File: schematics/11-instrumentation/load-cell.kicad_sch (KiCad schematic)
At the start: 12 parts, among them IC1 HX711, Q1 S8550

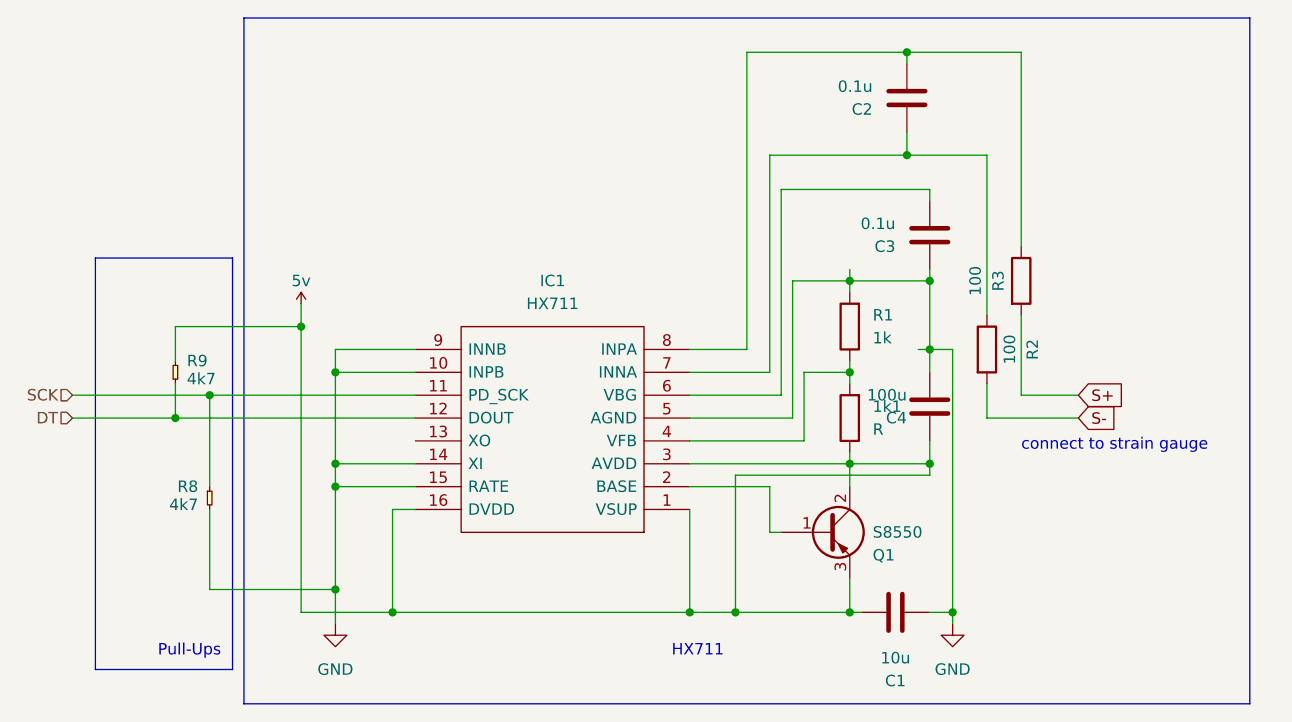
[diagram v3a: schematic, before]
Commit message: load cell schematic
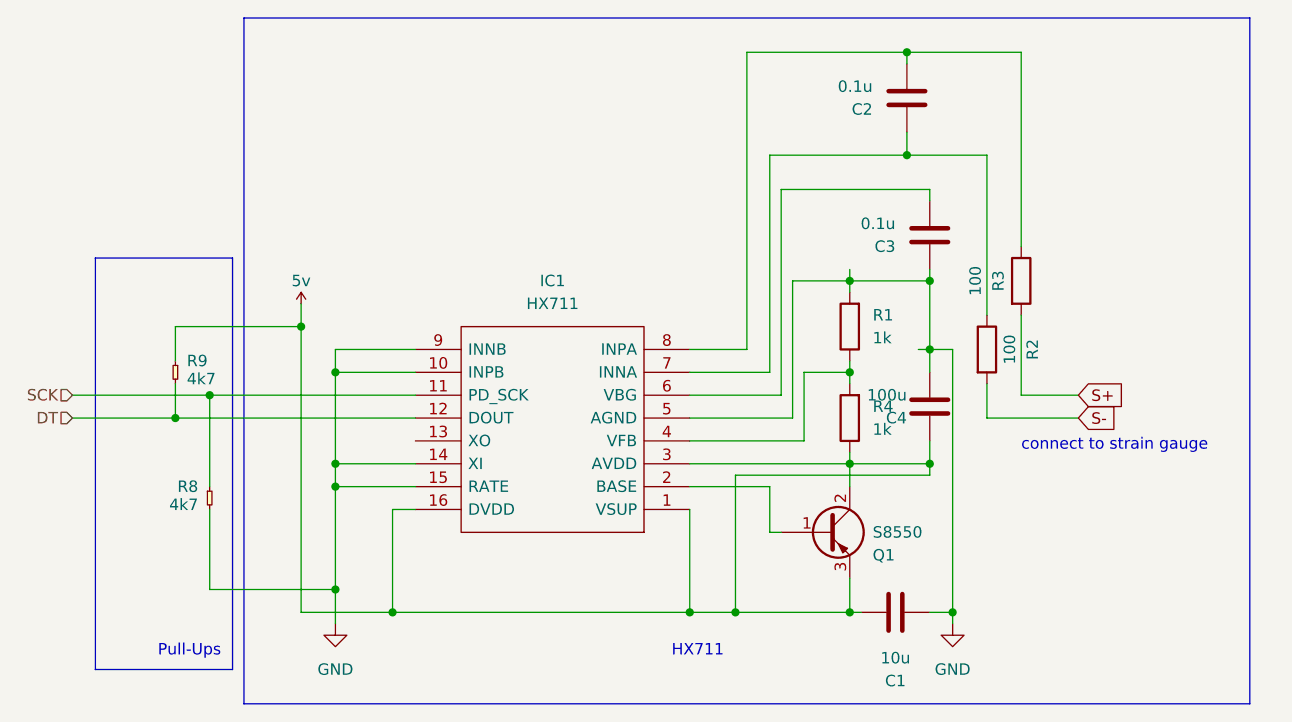
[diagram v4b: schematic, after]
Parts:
- C1, C2, C3, C4: footprint (none) -> royale:C_0402_1005Metric_Pad0.74x0.62mm_HandSolder
- IC1: footprint SOIC127P600X160-16N -> hx711:SOIC127P600X160-16N
- Q1: footprint (none) -> s8850:MJE13001TP
- R1, R2, R3, R8, R9: footprint (none) -> royale:R_0402_1005Metric_Pad0.72x0.64mm_HandSolder
- R4: renamed from 1k1; value R -> 1k; footprint (none) -> royale:R_0402_1005Metric_Pad0.72x0.64mm_HandSolder
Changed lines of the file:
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@@
+    (stroke (width 0) (type default) (color 0 0 0 0))
+  )
+  (wire (pts (xy 170.18 95.25) (xy 170.18 96.52))
     (stroke (width 0) (type default) (color 0 0 0 0))
   )
@@
     (stroke (width 0) (type default) (color 0 0 0 0))
   )
+  (wire (pts (xy 152.4 96.52) (xy 170.18 96.52))
+    (stroke (width 0) (type default) (color 0 0 0 0))
+  )
   (wire (pts (xy 119.38 101.6) (xy 119.38 113.03))
     (stroke (width 0) (type default) (color 0 0 0 0))
@@
     (stroke (width 0) (type default) (color 0 0 0 0))
   )
-  (wire (pts (xy 170.18 96.52) (xy 170.18 95.25))
-    (stroke (width 0) (type default) (color 0 0 0 0))
-  )
   (wire (pts (xy 181.61 83.82) (xy 179.07 83.82))
     (stroke (width 0) (type default) (color 0 0 0 0))
@@
   )
   (wire (pts (xy 162.56 88.9) (xy 152.4 88.9))
-    (stroke (width 0) (type default) (color 0 0 0 0))
-  )
-  (wire (pts (xy 170.18 96.52) (xy 152.4 96.52))
     (stroke (width 0) (type default) (color 0 0 0 0))
   )
@@
       (effects (font (size 1.27 1.27)) (justify left top))
     )
-    (property "Footprint" "" (id 2) (at 95.25 85.09 0)
+    (property "Footprint" "royale:R_0402_1005Metric_Pad0.72x0.64mm_HandSolder" (id 2) (at 95.25 85.09 0)
       (effects (font (size 1.27 1.27)) hide)
     )
@@
       (effects (font (size 1.27 1.27)) (justify left top))
     )
-    (property "Footprint" "" (id 2) (at 99.06 99.06 0)
+    (property "Footprint" "royale:R_0402_1005Metric_Pad0.72x0.64mm_HandSolder" (id 2) (at 99.06 99.06 0)
       (effects (font (size 1.27 1.27)) hide)
     )
@@
       (effects (font (size 1.27 1.27)) (justify left))
     )
-    (property "Footprint" "" (id 2) (at 178.1048 86.36 0)
+    (property "Footprint" "royale:C_0402_1005Metric_Pad0.74x0.62mm_HandSolder" (id 2) (at 178.1048 86.36 0)
       (effects (font (size 1.27 1.27)) hide)
     )
@@
       (effects (font (size 1.27 1.27)) (justify left))
     )
-    (property "Footprint" "" (id 2) (at 178.1048 67.31 0)
+    (property "Footprint" "royale:C_0402_1005Metric_Pad0.74x0.62mm_HandSolder" (id 2) (at 178.1048 67.31 0)
       (effects (font (size 1.27 1.27)) hide)
     )
@@
     (property "Reference" "R3" (id 0) (at 186.69 76.2 90))
     (property "Value" "100" (id 1) (at 184.15 76.2 90))
-    (property "Footprint" "" (id 2) (at 187.452 76.2 90)
+    (property "Footprint" "royale:R_0402_1005Metric_Pad0.72x0.64mm_HandSolder" (id 2) (at 187.452 76.2 90)
       (effects (font (size 1.27 1.27)) hide)
     )
@@
     (property "Reference" "IC1" (id 0) (at 137.16 76.2 0))
     (property "Value" "HX711" (id 1) (at 137.16 78.74 0))
-    (property "Footprint" "SOIC127P600X160-16N" (id 2) (at 125.73 104.14 0)
+    (property "Footprint" "hx711:SOIC127P600X160-16N" (id 2) (at 125.73 104.14 0)
       (effects (font (size 1.27 1.27)) (justify left) hide)
     )
@@
       (effects (font (size 1.27 1.27)) (justify left))
     )
-    (property "Footprint" "" (id 2) (at 172.72 101.6 0)
+    (property "Footprint" "s8850:MJE13001TP" (id 2) (at 172.72 101.6 0)
       (effects (font (size 1.27 1.27)) hide)
     )
@@
       (effects (font (size 1.27 1.27)) (justify left))
     )
-    (property "Footprint" "" (id 2) (at 175.5648 52.07 0)
+    (property "Footprint" "royale:C_0402_1005Metric_Pad0.74x0.62mm_HandSolder" (id 2) (at 175.5648 52.07 0)
       (effects (font (size 1.27 1.27)) hide)
     )
@@
   )
   (symbol (lib_id "Device:R") (at 170.18 91.44 180) (unit 1)
-    (in_bom yes) (on_board yes) (fields_autoplaced)
-    (property "Reference" "1k1" (id 0) (at 172.72 90.1699 0)
+    (in_bom yes) (on_board yes)
+    (property "Reference" "R4" (id 0) (at 172.72 90.1699 0)
       (effects (font (size 1.27 1.27)) (justify right))
     )
-    (property "Value" "R" (id 1) (at 172.72 92.7099 0)
+    (property "Value" "1k" (id 1) (at 172.72 92.7099 0)
       (effects (font (size 1.27 1.27)) (justify right))
     )
-    (property "Footprint" "" (id 2) (at 171.958 91.44 90)
+    (property "Footprint" "royale:R_0402_1005Metric_Pad0.72x0.64mm_HandSolder" (id 2) (at 171.958 91.44 90)
       (effects (font (size 1.27 1.27)) hide)
     )
@@
       (effects (font (size 1.27 1.27)) (justify right))
     )
-    (property "Footprint" "" (id 2) (at 171.958 81.28 90)
+    (property "Footprint" "royale:R_0402_1005Metric_Pad0.72x0.64mm_HandSolder" (id 2) (at 171.958 81.28 90)
       (effects (font (size 1.27 1.27)) hide)
     )
@@
     (property "Reference" "R2" (id 0) (at 190.5 83.82 90))
     (property "Value" "100" (id 1) (at 187.96 83.82 90))
-    (property "Footprint" "" (id 2) (at 183.642 83.82 90)
+    (property "Footprint" "royale:R_0402_1005Metric_Pad0.72x0.64mm_HandSolder" (id 2) (at 183.642 83.82 90)
       (effects (font (size 1.27 1.27)) hide)
     )
@@
     (property "Reference" "C1" (id 0) (at 175.26 120.65 90))
     (property "Value" "10u" (id 1) (at 175.26 118.11 90))
-    (property "Footprint" "" (id 2) (at 171.45 113.9952 0)
+    (property "Footprint" "royale:C_0402_1005Metric_Pad0.74x0.62mm_HandSolder" (id 2) (at 171.45 113.9952 0)
       (effects (font (size 1.27 1.27)) hide)
     )
@@
       (reference "#PWR0102") (unit 1) (value "GND") (footprint "")
     )
+    (path "/f1201ca4-ca7a-49b1-973f-66f02d485f1e"
+      (reference "C1") (unit 1) (value "10u") (footprint "royale:C_0402_1005Metric_Pad0.74x0.62mm_HandSolder")
+    )
+    (path "/d82854f8-978b-4c32-9d4b-da5e6d4de9ec"
+      (reference "C2") (unit 1) (value "0.1u") (footprint "royale:C_0402_1005Metric_Pad0.74x0.62mm_HandSolder")
+    )
+    (path "/3d0f2f77-1de1-4f89-8f9a-bc30dd32b34b"
+      (reference "C3") (unit 1) (value "0.1u") (footprint "royale:C_0402_1005Metric_Pad0.74x0.62mm_HandSolder")
+    )
+    (path "/36776052-bc85-446c-9b44-47290a9abc9f"
+      (reference "C4") (unit 1) (value "100u") (footprint "royale:C_0402_1005Metric_Pad0.74x0.62mm_HandSolder")
+    )
+    (path "/ab488037-0bdc-49ef-a068-f0a9c636318a"
+      (reference "IC1") (unit 1) (value "HX711") (footprint "hx711:SOIC127P600X160-16N")
+    )
+    (path "/b799addf-6933-4c44-bf61-27973e36aa81"
+      (reference "Q1") (unit 1) (value "S8550") (footprint "s8850:MJE13001TP")
+    )
+    (path "/da162b48-30bb-4fb8-b49b-4597c43d34c7"
+      (reference "R1") (unit 1) (value "1k") (footprint "royale:R_0402_1005Metric_Pad0.72x0.64mm_HandSolder")
+    )
+    (path "/e23a3038-169d-44ac-a06a-b2ed0b90cdbb"
+      (reference "R2") (unit 1) (value "100") (footprint "royale:R_0402_1005Metric_Pad0.72x0.64mm_HandSolder")
+    )
+    (path "/917c77a4-2bcc-4569-a027-3087491fca76"
+      (reference "R3") (unit 1) (value "100") (footprint "royale:R_0402_1005Metric_Pad0.72x0.64mm_HandSolder")
+    )
     (path "/d91d914d-cd2d-4fe2-b31b-1921e7526d9c"
-      (reference "1k1") (unit 1) (value "R") (footprint "")
-    )
-    (path "/f1201ca4-ca7a-49b1-973f-66f02d485f1e"
-      (reference "C1") (unit 1) (value "10u") (footprint "")
-    )
-    (path "/d82854f8-978b-4c32-9d4b-da5e6d4de9ec"
-      (reference "C2") (unit 1) (value "0.1u") (footprint "")
-    )
-    (path "/3d0f2f77-1de1-4f89-8f9a-bc30dd32b34b"
-      (reference "C3") (unit 1) (value "0.1u") (footprint "")
-    )
-    (path "/36776052-bc85-446c-9b44-47290a9abc9f"
-      (reference "C4") (unit 1) (value "100u") (footprint "")
-    )
-    (path "/ab488037-0bdc-49ef-a068-f0a9c636318a"
-      (reference "IC1") (unit 1) (value "HX711") (footprint "SOIC127P600X160-16N")
-    )
-    (path "/b799addf-6933-4c44-bf61-27973e36aa81"
-      (reference "Q1") (unit 1) (value "S8550") (footprint "")
-    )
-    (path "/da162b48-30bb-4fb8-b49b-4597c43d34c7"
-      (reference "R1") (unit 1) (value "1k") (footprint "")
-    )
-    (path "/e23a3038-169d-44ac-a06a-b2ed0b90cdbb"
-      (reference "R2") (unit 1) (value "100") (footprint "")
-    )
-    (path "/917c77a4-2bcc-4569-a027-3087491fca76"
-      (reference "R3") (unit 1) (value "100") (footprint "")
+      (reference "R4") (unit 1) (value "1k") (footprint "royale:R_0402_1005Metric_Pad0.72x0.64mm_HandSolder")
     )
     (path "/00000000-0000-0000-0000-000062708e6f"
-      (reference "R8") (unit 1) (value "4k7") (footprint "")
+      (reference "R8") (unit 1) (value "4k7") (footprint "royale:R_0402_1005Metric_Pad0.72x0.64mm_HandSolder")
     )
     (path "/00000000-0000-0000-0000-000062708e69"
-      (reference "R9") (unit 1) (value "4k7") (footprint "")
-    )
-  )
+      (reference "R9") (unit 1) (value "4k7") (footprint "royale:R_0402_1005Metric_Pad0.72x0.64mm_HandSolder")
+    )
+  )
